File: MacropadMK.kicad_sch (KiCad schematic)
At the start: 42 parts, among them J1 BME280, SHT40 Module, J10 SCD40 Module, J11 Conn_01x03, J12 Conn_01x03, J13 SCD40 Module, J14 BME280, SHT40 Module, J15 mmWave Connector, J16 mmWave Connector, J17 mmWave Connector, J2 SCD40 Module, J3 Conn_01x02, J4 Qwiic_Vertical, J5 Conn_01x02, J6 Conn_01x02, J7 Conn_01x03, J8 Conn_01x03, J9 VL53L0X Module, Q1 PT19-21C, U5 TLP175A

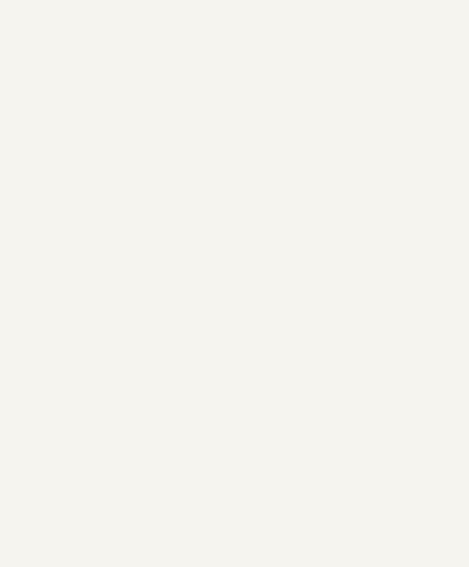
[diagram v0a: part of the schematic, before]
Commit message: Add updated ESP32-S3-Zero footprint
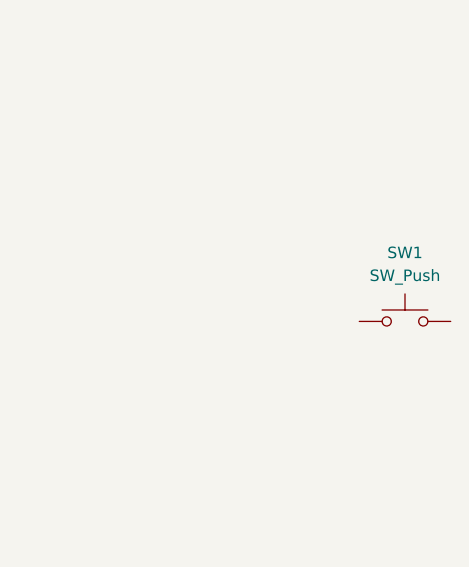
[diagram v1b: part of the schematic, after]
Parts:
- added SW1: SW_Push, Button_Switch_Keyboard:SW_Cherry_MX_1.00u_PCB, symbol Switch:SW_Push
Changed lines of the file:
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@@
+	)
+	(symbol
+		(lib_id "Switch:SW_Push")
+		(at 344.17 114.3 0)
+		(unit 1)
+		(body_style 1)
+		(exclude_from_sim no)
+		(in_bom yes)
+		(on_board yes)
+		(in_pos_files yes)
+		(dnp no)
+		(fields_autoplaced yes)
+		(property "Reference" "SW1"
+			(at 344.17 106.68 0)
+			(show_name no)
+			(do_not_autoplace no)
+			(effects
+				(font
+					(size 1.27 1.27)
+				)
+			)
+		)
+		(property "Value" "SW_Push"
+			(at 344.17 109.22 0)
+			(show_name no)
+			(do_not_autoplace no)
+			(effects
+				(font
+					(size 1.27 1.27)
+				)
+			)
+		)
+		(property "Footprint" "Button_Switch_Keyboard:SW_Cherry_MX_1.00u_PCB"
+			(at 344.17 109.22 0)
+			(hide yes)
+			(show_name no)
+			(do_not_autoplace no)
+			(effects
+				(font
+					(size 1.27 1.27)
+				)
+			)
+		)
+		(property "Datasheet" ""
+			(at 344.17 109.22 0)
+			(hide yes)
+			(show_name no)
+			(do_not_autoplace no)
+			(effects
+				(font
+					(size 1.27 1.27)
+				)
+			)
+		)
+		(property "Description" "Push button switch, generic, two pins"
+			(at 344.17 114.3 0)
+			(hide yes)
+			(show_name no)
+			(do_not_autoplace no)
+			(effects
+				(font
+					(size 1.27 1.27)
+				)
+			)
+		)
+		(pin "2"
+		)
+		(pin "1"
+		)
+		(instances
+			(project "MacropadMK"
+				(path "/8aac3481-571f-4367-bd23-185f621364a9"
+					(reference "SW1")
+					(unit 1)
+				)
+			)
+		)
 	)
 	(symbol

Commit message: added librarys
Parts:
- removed J1, J14: BME280, SHT40 Module, PCM_SparkFun-Connector:1x04_P2.54mm, symbol PCM_SparkFun-Connector:Conn_01x04_P2.54mm
- removed J10, J13, J2: SCD40 Module, PCM_SparkFun-Connector:1x04_P2.54mm, symbol PCM_SparkFun-Connector:Conn_01x04_P2.54mm
- removed J11, J12, J7, J8: Conn_01x03, PCM_SparkFun-Connector:1x03_P2.54mm, symbol PCM_SparkFun-Connector:Conn_01x03_P2.54mm
- removed J17: mmWave Connector, PCM_SparkFun-Connector:JST_1x04_P1.0mm_Vertical_SMD, symbol PCM_SparkFun-Connector:Qwiic_Vertical
- removed J3, J5, J6: Conn_01x02, PCM_SparkFun-Connector:1x02_P2.54mm, symbol PCM_SparkFun-Connector:Conn_01x02_P2.54mm
- removed J9: VL53L0X Module, PCM_SparkFun-Connector:1x04_P2.54mm, symbol PCM_SparkFun-Connector:Conn_01x04_P2.54mm
- removed Q1: PT19-21C, LED_SMD:LED_0603_1608Metric, symbol Device:Q_Photo_NPN
- removed R1, R2: 4k7, Resistor_SMD:R_0805_2012Metric, symbol Device:R
- removed R10, R11, R12, R6, R7, R8: 470R, Resistor_SMD:R_0805_2012Metric, symbol Device:R
- removed R13, R14, R15: 2k2, Resistor_SMD:R_0805_2012Metric, symbol Device:R
- removed R5: 10k, Resistor_SMD:R_0805_2012Metric, symbol Device:R
- removed U2: (no value), MacropadMK_Sensor_Footprints:HLK-LD2410B-mmWave-Sensor, symbol MacropadMK_Sensor_Symbols:HLK-LD2410B-mmWave-Sensor
- removed U4: (no value), MacropadMK_Sensor_Footprints:SR602-PIR-Motion-Sensor, symbol MacropadMK_Sensor_Symbols:SR602-PIR-Motion-Sensor
- removed U5: TLP175A, Package_SO:Toshiba_SOIC-4-6_4.4x3.6mm_P1.27mm, symbol Relay_SolidState:TLP175A
- U1: footprint MacropadMK_Custom_Footprints:ESP32-S3-Zero -> ProjectFootprints:ESP32-S3-Zero_Hybrid_BottomLabels
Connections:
- net PIR is gone; now on net SCK: U1.16 (GPIO13)
- net Relais is gone; now on net SDA: U1.15 (GPIO12)
- net SCK: no longer U1.12 (GP9)
- net SDA: no longer U1.11 (GP8)
- net UART_RX_mmWAVE: now also U1.26 (GPIO17); no longer U1.13 (GP10)
- net UART_TX_mmWAVE: now also U1.25 (GPIO18); no longer U1.14 (GP11)
- net WS12_LED_IN: no longer U1.10 (GP7)
- net GPIO_1: no longer names the net of U1.4 (GPIO1)
- net GPIO_2: no longer names the net of U1.5 (GPIO2)
- net GPIO_4: no longer names the net of U1.7 (GPIO4)
- net GPIO_5: no longer names the net of U1.8 (GPIO5)
- net GPIO_6: no longer names the net of U1.9 (GPIO6)
- net PhotoMeas: no longer names the net of U1.6 (GPIO3)
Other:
- note removed: "GPIOs"
- note removed: "I2C Modules"
- note removed: "PIR sensor"
- note removed: "Phototransistor"
- note removed: "mmWave"
- note removed: "solid state relais"
- note removed: "supply pins"
- moved on the sheet: J15, J16

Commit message: add librarys
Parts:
- added D3: 1N4148W, Diode_SMD:D_SOD-123, symbol Diode:1N4148W
- added SW2, SW3, SW4: SW_Push, Button_Switch_Keyboard:SW_Cherry_MX_1.00u_PCB, symbol Switch:SW_Push
- U1: footprint ProjectFootprints:ESP32-S3-Zero_Hybrid_BottomLabels -> MacropadMK_Custom_Footprints:ESP32-S3-Zero
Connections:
- net at SW1.2: now also D3.1 (K)
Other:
- moved on the sheet: C1, C2, C3, J4, R3, R4, R9, SW1

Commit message: Add project-local KiCad libraries and update schematic
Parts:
- removed J15, J16: mmWave Connector, PCM_SparkFun-Connector:JST_1x04_P1.0mm_Vertical_SMD, symbol PCM_SparkFun-Connector:Qwiic_Vertical
- added D10, D11, D12, D13, D14, D4, D5, D6, D7, D8, D9: 1N4148W, Diode_SMD:D_SOD-123, symbol Diode:1N4148W
- added DS1: OLED_SSD1306_0.96in_128x64_I2C, SSD1306_OLED:OLED_SSD1306_0.96in_128x64_I2C, symbol SSD1306_OLED:OLED_SSD1306_0.96in_128x64_I2C
- added J5: Qwiic_Vertical, Connector_JST:JST_SH_BM04B-SRSS-TB_1x04-1MP_P1.00mm_Vertical, symbol PCM_SparkFun-Connector:Qwiic_Vertical
- added R5, R6, R7: 2k2, Resistor_SMD:R_0805_2012Metric, symbol Device:R
- added SW10, SW11, SW12, SW5, SW6, SW7, SW8, SW9: SW_Push, Keyswitch_Cherry_MX:SW_Cherry_MX_PCB_1.00u, symbol Switch:SW_Push
- J4: footprint PCM_SparkFun-Connector:JST_1x04_P1.0mm_Vertical_SMD -> Connector_JST:JST_SH_BM04B-SRSS-TB_1x04-1MP_P1.00mm_Vertical
- SW1, SW2, SW3, SW4: footprint Button_Switch_Keyboard:SW_Cherry_MX_1.00u_PCB -> Keyswitch_Cherry_MX:SW_Cherry_MX_PCB_1.00u
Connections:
- net +3V3: now also R5.2, R6.2, R7.2
- net +5V: now also DS1.2 (VCC), J5.4 (Pin_4)
- net COL1: now also SW1.2, SW4.2, U1.4 (GPIO1), R5.1, SW10.2, SW7.2
- net GND: now also DS1.1 (GND), J5.1 (Pin_1)
- net SCK: now also DS1.3 (SCL)
- net SDA: now also DS1.4 (SDA)
- net UART_RX_mmWAVE: now also J5.2 (Pin_2)
- net UART_TX_mmWAVE: now also J5.3 (Pin_3)
- net at SW2.1: now also D5.2 (A)
- net COL2: now reaches SW2.2
- net COL2: now also U1.5 (GPIO2), R6.1, SW11.2, SW5.2, SW8.2
- net ROW4: now reaches U1.10 (GPIO7)
- net ROW4: now also D12.1 (K), D13.1 (K), D14.1 (K)
- net COL3: now reaches U1.6 (GPIO3)
- net COL3: now also SW3.2, R7.1, SW12.2, SW6.2, SW9.2
- net ROW1: now reaches U1.7 (GPIO4)
- net ROW1: now also D3.1 (K), D5.1 (K), D6.1 (K)
- net ROW2: now reaches U1.8 (GPIO5)
- net ROW2: now also D4.1 (K), D7.1 (K), D8.1 (K)
- net ROW3: now reaches U1.9 (GPIO6)
- net ROW3: now also D10.1 (K), D11.1 (K), D9.1 (K)
- net at D3.2 (A): now also SW1.1
- net at SW4.1: now also D4.2 (A)
- net at SW3.1: now also D6.2 (A)
- new net: D11.2 (A), SW9.1
- new net: D14.2 (A), SW12.1
- new net: D8.2 (A), SW6.1
- new net: D7.2 (A), SW5.1
- new net: J5.NC1 (NC), J5.NC2 (NC)
- new net: D13.2 (A), SW11.1
- new net: D9.2 (A), SW7.1
- new net: D10.2 (A), SW8.1
- new net: D12.2 (A), SW10.1
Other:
- note removed: "QWIIC connector"
- moved on the sheet: C1, C2, C3, J4, R3, R4, R9

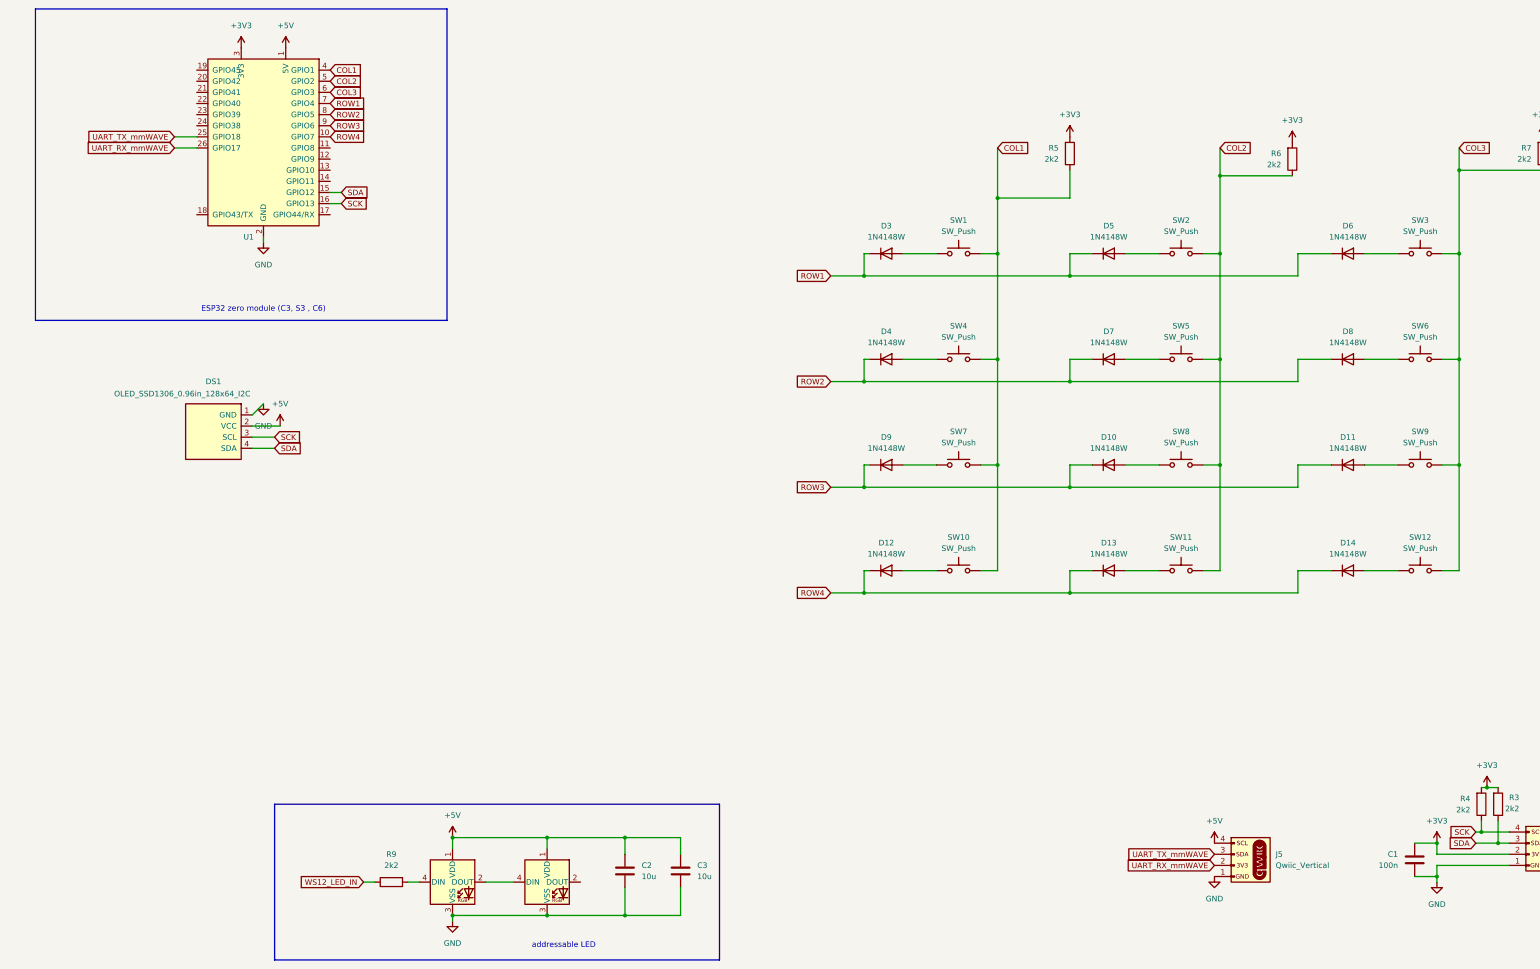
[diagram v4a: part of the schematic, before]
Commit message: Save complete KiCad project state
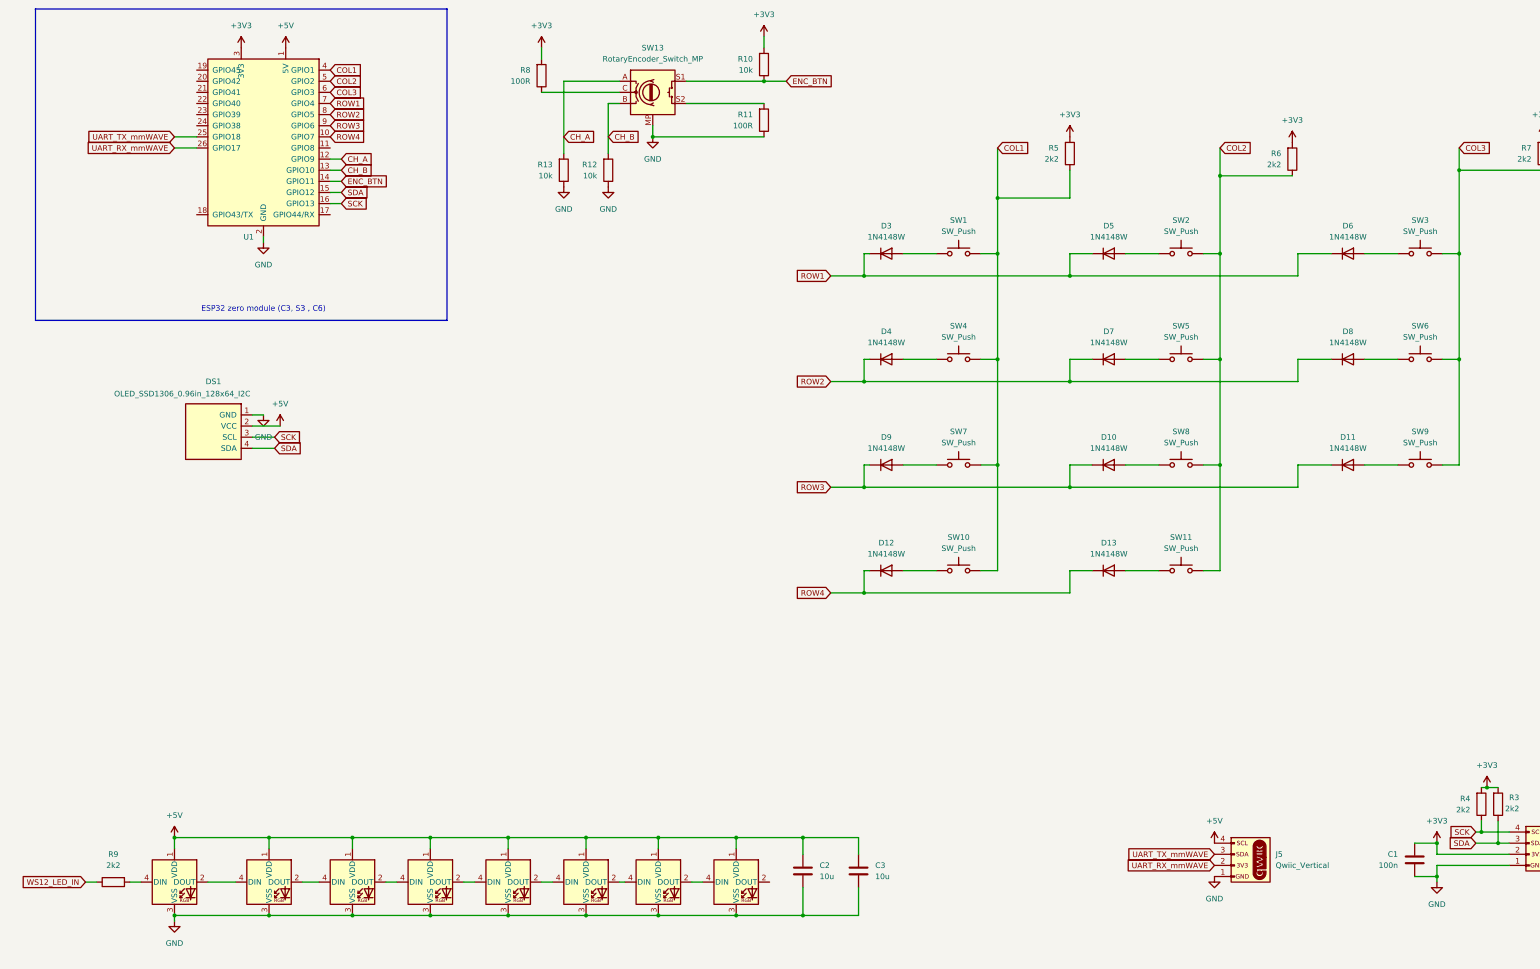
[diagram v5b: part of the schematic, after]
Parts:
- removed D14: 1N4148W, Diode_SMD:D_SOD-123, symbol Diode:1N4148W
- removed SW12: SW_Push, Keyswitch_Cherry_MX:SW_Cherry_MX_PCB_1.00u, symbol Switch:SW_Push
- added D14, D15, D16, D17, D18, D19: WS2812B, LED_SMD:LED_WS2812B_PLCC4_5.0x5.0mm_P3.2mm, symbol LED:WS2812B
- added R10, R12, R13: 10k, Resistor_SMD:R_0805_2012Metric, symbol Device:R
- added R11, R8: 100R, Resistor_SMD:R_0805_2012Metric, symbol Device:R
- added SW13: RotaryEncoder_Switch_MP, Rotary_Encoder:RotaryEncoder_Alps_EC11E-Switch_Vertical_H20mm, symbol Device:RotaryEncoder_Switch_MP
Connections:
- net +3V3: now also R10.2, R8.2
- net +5V: now also D14.1 (VDD), D15.1 (VDD), D16.1 (VDD), D17.1 (VDD), D18.1 (VDD), D19.1 (VDD)
- net GND: now also D14.3 (VSS), D15.3 (VSS), D16.3 (VSS), D17.3 (VSS), D18.3 (VSS), D19.3 (VSS), R11.1, R12.1, R13.1, SW13.MP
- net CH_A: now reaches U1.12 (GPIO9)
- net CH_A: now also R13.2, SW13.A
- net CH_B: now reaches U1.13 (GPIO10)
- net CH_B: now also R12.2, SW13.B
- net ENC_BTN: now reaches U1.14 (GPIO11)
- net ENC_BTN: now also R10.1, SW13.S1
- net at D2.2 (DOUT): now also D14.4 (DIN)
- new net: R8.1, SW13.C
- new net: R11.2, SW13.S2
- new net: D18.2 (DOUT), D19.4 (DIN)
- new net: D14.2 (DOUT), D15.4 (DIN)
- new net: D17.2 (DOUT), D18.4 (DIN)
- new net: D15.2 (DOUT), D16.4 (DIN)
- new net: D16.2 (DOUT), D17.4 (DIN)
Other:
- note removed: "addressable LED"
- moved on the sheet: C2, C3, R9

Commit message: first try of layout
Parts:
- added H1, H2, H3, H4: MountingHole, MountingHole:MountingHole_3.2mm_M3, symbol Mechanical:MountingHole
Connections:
- net WS12_LED_IN: now also U1.11 (GPIO8)

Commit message: first version with all features
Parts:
- removed R3, R4, R5, R6, R7: 2k2, Resistor_SMD:R_0805_2012Metric, symbol Device:R
- removed R8: 100R, Resistor_SMD:R_0805_2012Metric, symbol Device:R
- added F1, F2: Fuse, Fuse:Fuse_0805_2012Metric, symbol Device:Fuse
- added J1: USB_C_Receptacle_USB2.0_16P_FLAT, Connector_USB:USB_C_Receptacle_HRO_TYPE-C-31-M-12, symbol Connector:USB_C_Receptacle_USB2.0_16P
- added J2: USB_C_Receptacle_USB2.0_16P_AXIAL, Connector_USB:USB_C_Receptacle_JAE_DX07S024WJ3R400, symbol Connector:USB_C_Receptacle_USB2.0_16P
- added R14, R15: 10k, Resistor_SMD:R_0201_0603Metric, symbol Device:R
- added R16, R17: 2k2, Resistor_SMD:R_0201_0603Metric, symbol Device:R
- added R18, R19, R20, R21: 5k1, Resistor_SMD:R_0201_0603Metric, symbol Device:R
- R10, R12, R13: footprint Resistor_SMD:R_0805_2012Metric -> Resistor_SMD:R_0201_0603Metric
- R11: value 100R -> 10k; footprint Resistor_SMD:R_0805_2012Metric -> Resistor_SMD:R_0201_0603Metric
- R9: footprint Resistor_SMD:R_0805_2012Metric -> Resistor_SMD:R_0603_1608Metric
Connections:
- net +3V3: now also R11.2, SW13.C, R14.2, R15.2, R16.2, R17.2
- net +5V: now also F1.2, F2.2
- net CH_A: now also R12.2; no longer R13.2
- net CH_B: now also R13.2; no longer R12.2
- net COL1: now also R11.1
- net COL2: now also R14.1
- net COL3: now also R15.1
- net GND: now also SW13.S2, J1.A1 (GND), J1.A12 (GND), J1.B1 (GND), J1.B12 (GND), J1.SH (SHIELD), J2.A1 (GND), J2.A12 (GND), J2.B1 (GND), J2.B12 (GND), J2.SH (SHIELD), R18.1, R19.1, R20.1, R21.1; no longer R11.1
- net SCK: now also R16.1
- net SDA: now also R17.1
- new net: F1.1, J1.A4 (VBUS), J1.A9 (VBUS), J1.B4 (VBUS), J1.B9 (VBUS)
- new net: J1.A5 (CC1), R19.2
- new net: J1.B5 (CC2), R18.2
- new net: F2.1, J2.A4 (VBUS), J2.A9 (VBUS), J2.B4 (VBUS), J2.B9 (VBUS)
- new net: J2.A5 (CC1), R21.2
- new net: J2.B5 (CC2), R20.2
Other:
- moved on the sheet: C2, C3, R9

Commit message: ready to order, all features prepared
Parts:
- added H5: MountingHole, MountingHole:MountingHole_3.2mm_M3, symbol Mechanical:MountingHole
- added J3, J6, J7: Conn_01x03_Pin, Connector_JST:JST_SH_BM03B-SRSS-TB_1x03-1MP_P1.00mm_Vertical, symbol Connector:Conn_01x03_Pin
- added R23, R24, R25, R26, R27, R28: 10k, Resistor_SMD:R_0201_0603Metric, symbol Device:R
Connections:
- net +3V3: now also J3.1 (Pin_1), J6.1 (Pin_1), J7.1 (Pin_1), R23.2, R25.2, R27.2
- net GND: now also J3.3 (Pin_3), J6.3 (Pin_3), J7.3 (Pin_3), R24.1, R26.1, R28.1
- net GPIO45: now reaches U1.19 (GPIO45)
- net GPIO45: now also J7.2 (Pin_2), R27.1, R28.2
- net GPIO42: now reaches U1.20 (GPIO42)
- net GPIO42: now also J3.2 (Pin_2), R23.1, R24.2
- net GPIO41: now reaches U1.21 (GPIO41)
- net GPIO41: now also J6.2 (Pin_2), R25.1, R26.2
